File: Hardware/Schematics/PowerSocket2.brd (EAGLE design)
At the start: 99 x 48.5 mm, 79 parts, among them IC1 REG1117, IC3 74AC373DW, J1 1X2-3.5MM, J2 1X2-3.5MM, J3 1X2-3.5MM, J4 1X2-3.5MM, J5 1X2-3.5MM, J6 1X2-3.5MM, J7 1X2-3.5MM, J8 1X2-3.5MM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

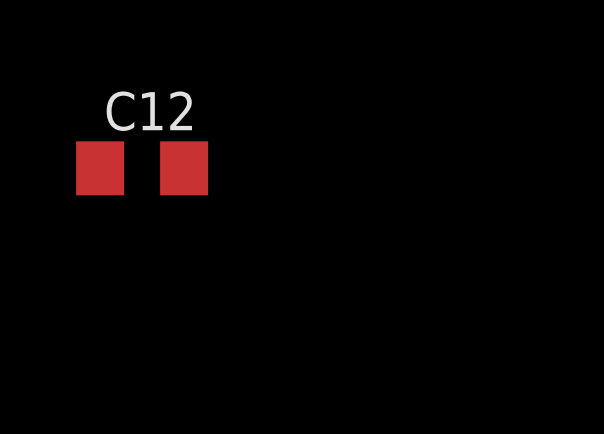
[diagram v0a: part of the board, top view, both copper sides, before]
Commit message: Fixed some issues in the schematic.
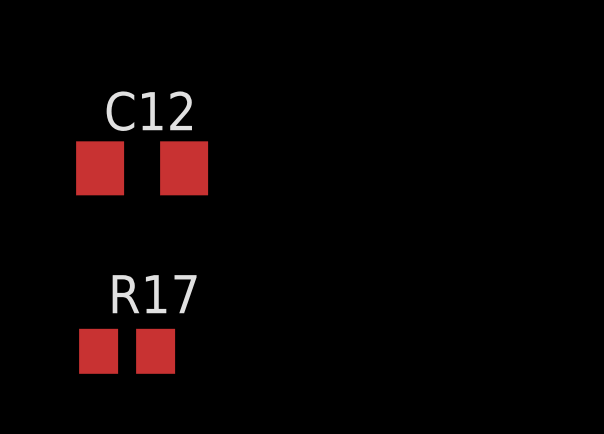
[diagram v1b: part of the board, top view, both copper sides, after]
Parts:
- added R17: 100K, rcl:R0805
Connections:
- net GND: now also IC3.13, IC3.14, IC3.17, IC3.18, IC3.8, R17.2
- net N$32: now also R17.1
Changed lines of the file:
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@@
 <element name="R16" library="resistor" library_urn="urn:adsk.eagle:library:348" package="0207/10" value="8.2K" x="-36.7" y="-564.2"/>
 <element name="C12" library="rcl" package="C1206" value="100nF" x="-45.9" y="-573.9"/>
+<element name="R17" library="rcl" package="R0805" value="100K" x="-46.4" y="-580"/>
 </elements>
 <signals>
@@
 <contactref element="HCPL-7520" pad="6"/>
 <contactref element="C12" pad="1"/>
-<wire x1="-37.29" y1="-436.75" x2="-30.815" y2="-445.7292" width="0" layer="19" extent="1-1"/>
+<contactref element="R17" pad="2"/>
+<contactref element="IC3" pad="18"/>
+<contactref element="IC3" pad="17"/>
+<contactref element="IC3" pad="14"/>
+<contactref element="IC3" pad="13"/>
+<contactref element="IC3" pad="8"/>
+<wire x1="-21.925" y1="-445.7292" x2="-30.815" y2="-445.7292" width="0" layer="19" extent="1-1"/>
+<wire x1="-19.385" y1="-445.7292" x2="-21.925" y2="-445.7292" width="0" layer="19" extent="1-1"/>
+<wire x1="-21.925" y1="-435.6708" x2="-21.925" y2="-445.7292" width="0" layer="19" extent="1-1"/>
+<wire x1="-23.195" y1="-435.6708" x2="-21.925" y2="-435.6708" width="0" layer="19" extent="1-1"/>
+<wire x1="-27.005" y1="-435.6708" x2="-23.195" y2="-435.6708" width="0" layer="19" extent="1-1"/>
+<wire x1="-28.275" y1="-435.6708" x2="-27.005" y2="-435.6708" width="0" layer="19" extent="1-1"/>
+<wire x1="-37.29" y1="-436.75" x2="-28.275" y2="-435.6708" width="0" layer="19" extent="1-1"/>
 <wire x1="-39.83" y1="-436.75" x2="-37.29" y2="-436.75" width="0" layer="19" extent="1-1"/>
-<wire x1="-19.385" y1="-445.7292" x2="-30.815" y2="-445.7292" width="0" layer="19" extent="1-1"/>
-<wire x1="-10.25" y1="-429.3" x2="-19.385" y2="-445.7292" width="0" layer="19" extent="1-1"/>
+<wire x1="-10.25" y1="-429.3" x2="-21.925" y2="-435.6708" width="0" layer="19" extent="1-1"/>
 <wire x1="3.605" y1="-410.9" x2="-10.25" y2="-429.3" width="0" layer="19" extent="1-1"/>
 <wire x1="19.05" y1="-408.4" x2="3.605" y2="-410.9" width="0" layer="19" extent="1-1"/>
@@
 <wire x1="85" y1="45" x2="62.8512" y2="42.7606" width="0" layer="19" extent="1-1"/>
 <wire x1="-47.3" y1="-573.9" x2="-30.815" y2="-445.7292" width="0" layer="19" extent="1-1"/>
+<wire x1="-45.45" y1="-580" x2="-47.3" y2="-573.9" width="0" layer="19" extent="1-1"/>
 </signal>
 <signal name="VCC">
@@
 <contactref element="U1" pad="5"/>
 <contactref element="IC3" pad="11"/>
+<contactref element="R17" pad="1"/>
+<wire x1="-47.35" y1="-580" x2="-19.385" y2="-435.6708" width="0" layer="19" extent="1-1"/>
 <wire x1="30.55" y1="19.99" x2="-19.385" y2="-435.6708" width="0" layer="19" extent="1-1"/>
 </signal>

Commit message: Return OK in settings.
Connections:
- net FLASH: now also U1.25; no longer U1.26
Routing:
- net FLASH: track 54.9 -> 54.1 mm
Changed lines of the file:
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@@
 <contactref element="R2" pad="2"/>
 <contactref element="FLASH" pad="3"/>
-<contactref element="U1" pad="26"/>
-<wire x1="11.3" y1="30.15" x2="12.05" y2="30.15" width="0.3048" layer="1"/>
 <wire x1="9.85" y1="31.6" x2="11.3" y2="30.15" width="0.3048" layer="1"/>
 <wire x1="49.0512" y1="38.2394" x2="42.5488" y2="38.2394" width="0.3048" layer="16"/>
@@
 <wire x1="29.2" y1="33.3" x2="22.9" y2="39.6" width="0.254" layer="16"/>
 <wire x1="22.9" y1="39.6" x2="9.7" y2="39.6" width="0.254" layer="16"/>
+<contactref element="U1" pad="25"/>
+<wire x1="11.3" y1="30.15" x2="12.05" y2="31.42" width="0" layer="19" extent="1-1"/>
 </signal>
 <signal name="GATE3">
